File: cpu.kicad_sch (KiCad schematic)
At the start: 28 parts, among them J81 Conn_01x03_Pin, J82 Conn_Coaxial, J83 Conn_Coaxial, J84 Conn_01x02_Pin, SW81 SW_Push, SW82 SW_Push, U8 ESP32-C6-MINI-1U, U81 74HC595, U82 74HC595, U84 ISOW7842

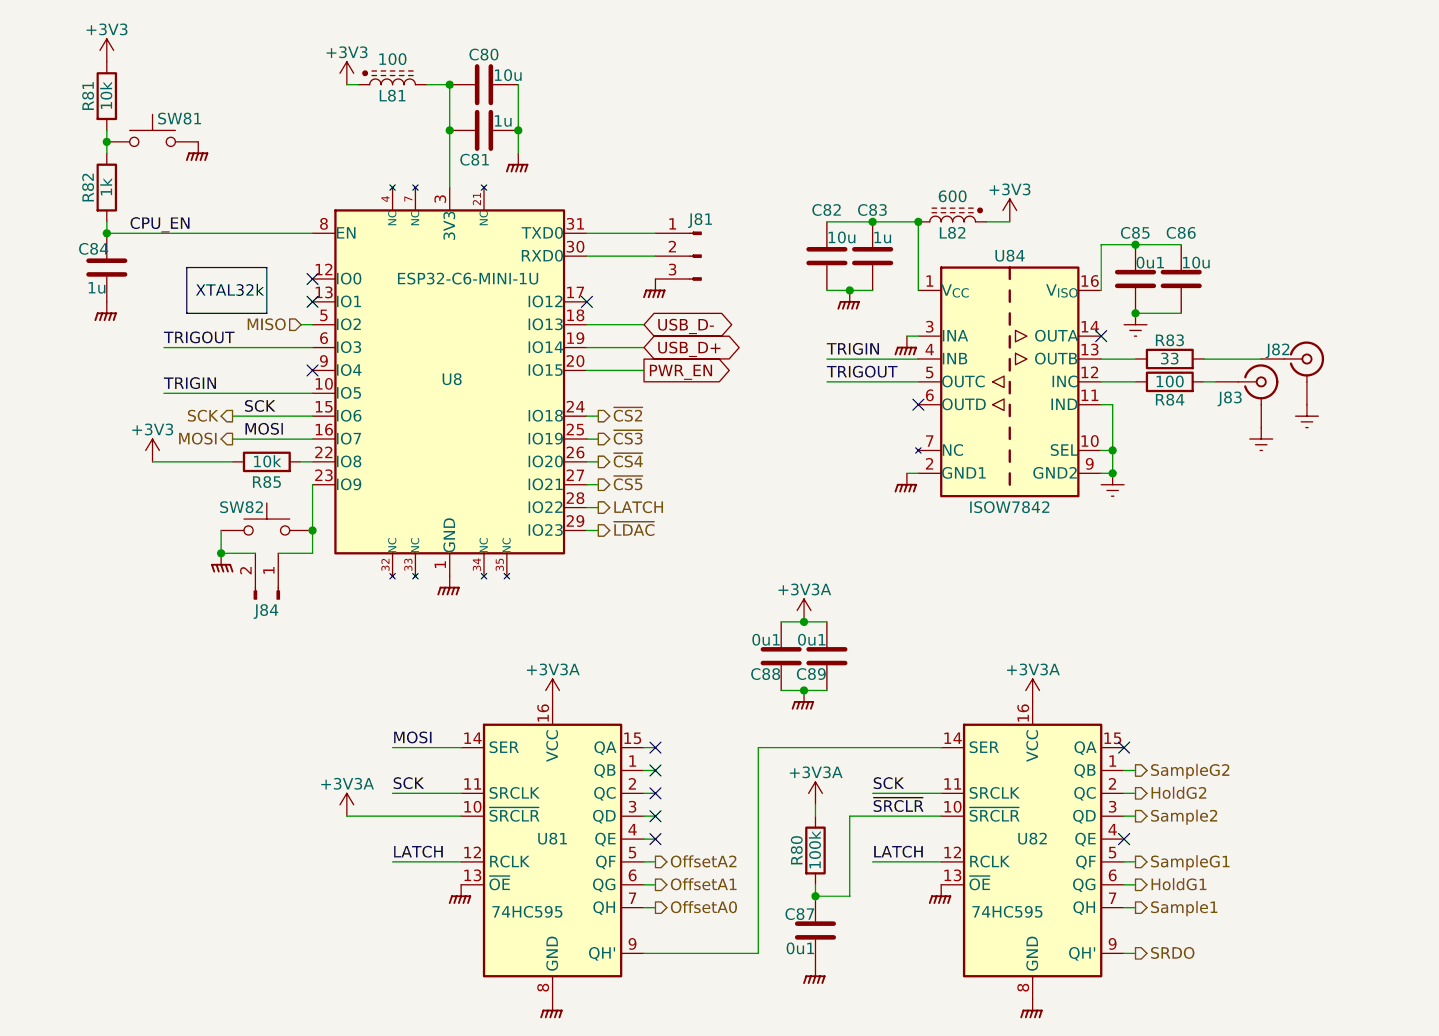
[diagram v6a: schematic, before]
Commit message: Power mostly routed
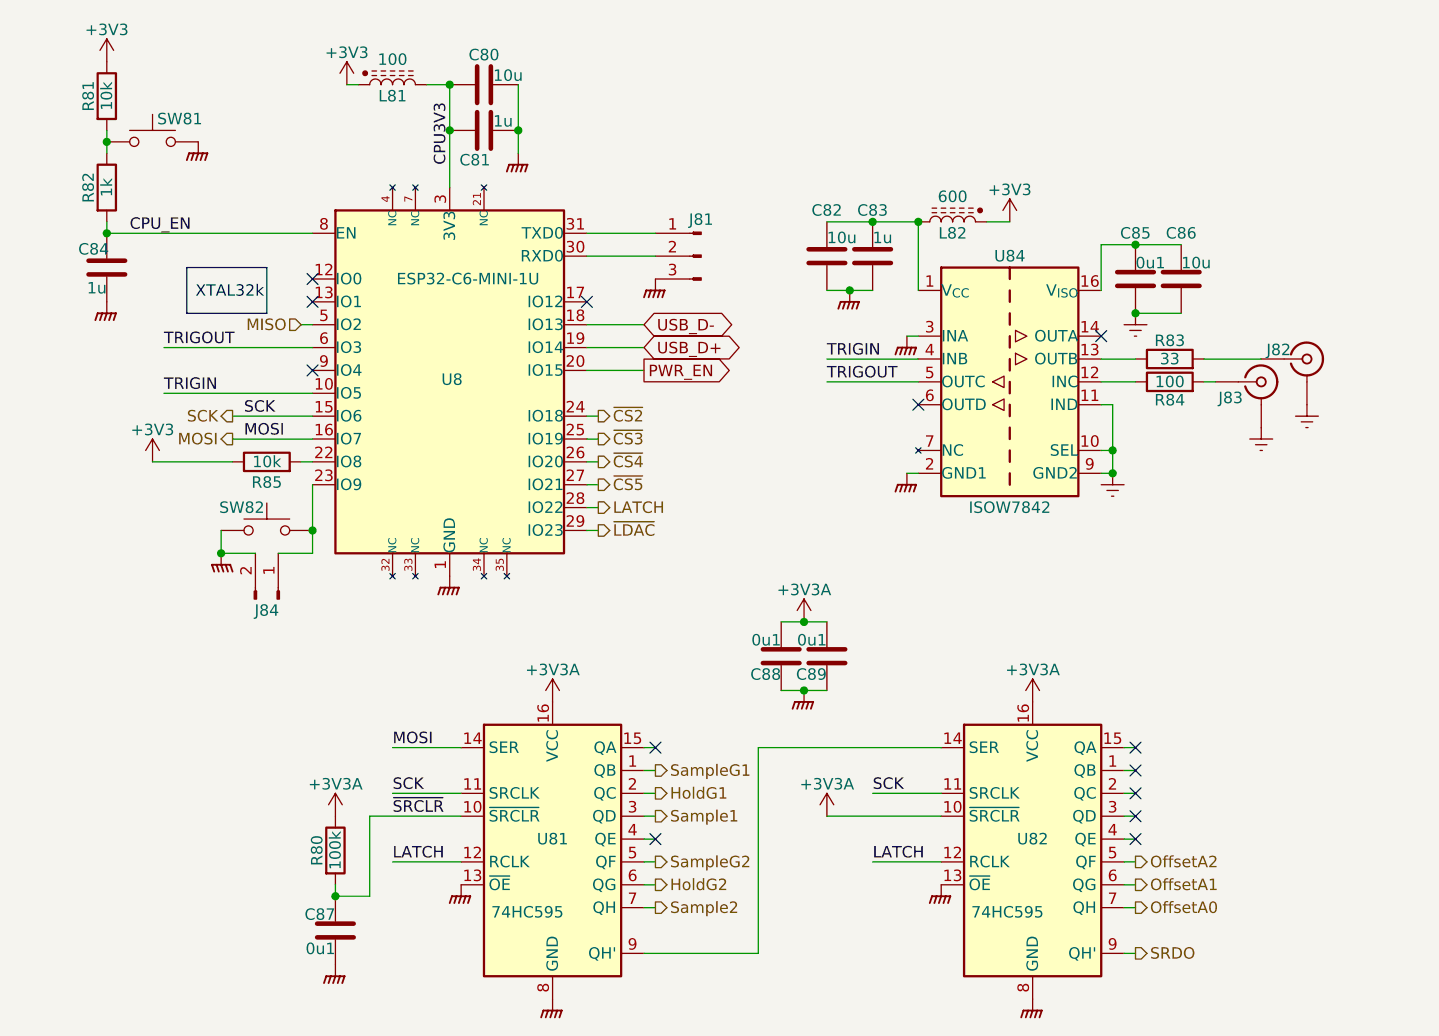
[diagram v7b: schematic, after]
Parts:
- renumbered U82 to U81, U81 to U82
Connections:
- net HoldG1: now also U81.2 (QC); no longer U81.6 (QG)
- net HoldG2: now also U81.6 (QG); no longer U81.2 (QC)
- net MOSI: now also U81.14 (SER); no longer U82.14 (SER)
- net SRDO: now also U82.9 (QH'); no longer U81.9 (QH')
- net Sample1: now also U81.3 (QD); no longer U81.7 (QH)
- net Sample2: now also U81.7 (QH); no longer U81.3 (QD)
- net SampleG1: now also U81.1 (QB); no longer U81.5 (QF)
- net SampleG2: now also U81.5 (QF); no longer U81.1 (QB)
- net CPU3V3: now reaches C80.1, C81.1, L81.2, U8.3 (3V3)
- new net: U81.9 (QH'), U82.14 (SER)
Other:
- moved on the sheet: C87, R80, U81, U82

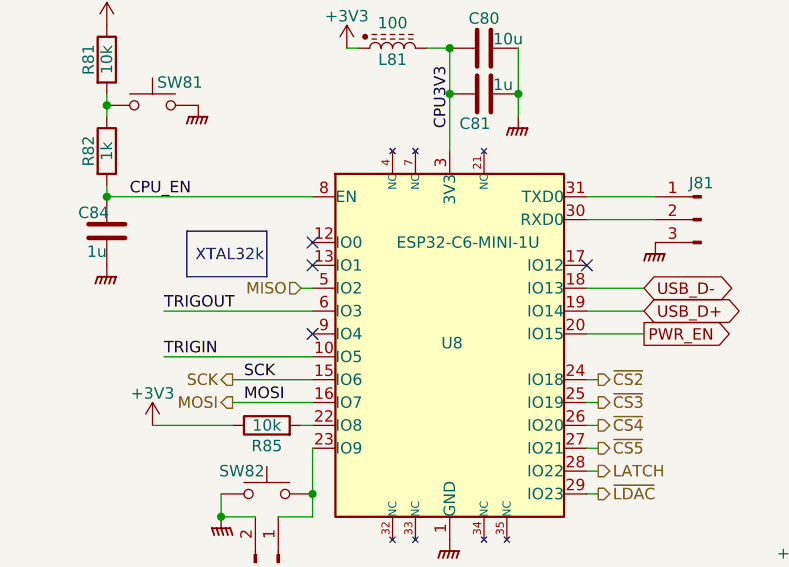
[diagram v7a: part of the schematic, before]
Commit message: Nearly all routed.  Repinning FDA resistors.
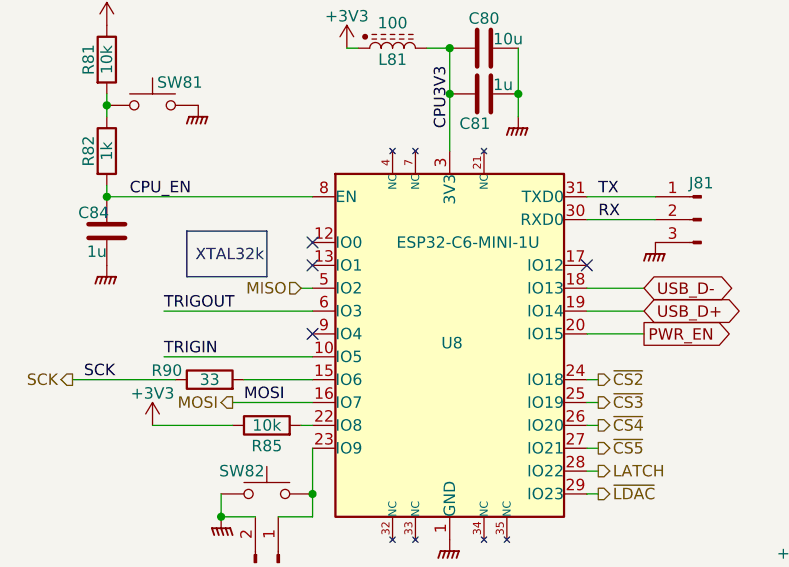
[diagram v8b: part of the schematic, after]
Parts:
- added R90: 33, Resistor_SMD:R_0402_1005Metric, symbol Device:R
- R80: LCSC (none) -> C25741
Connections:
- net SCK: now also R90.1; no longer U8.15 (IO6)
- net TX: now reaches J81.1 (Pin_1), U8.31 (TXD0)
- net RX: now reaches J81.2 (Pin_2), U8.30 (RXD0)
- new net: R90.2, U8.15 (IO6)
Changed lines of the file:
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@@
 	(wire
 		(pts
-			(xy 71.12 68.58) (xy 80.01 68.58)
+			(xy 53.34 68.58) (xy 64.77 68.58)
 		)
 		(stroke
@@
 	(wire
 		(pts
+			(xy 72.39 68.58) (xy 80.01 68.58)
+		)
+		(stroke
+			(width 0)
+			(type default)
+		)
+	)
+	(wire
+		(pts
 			(xy 110.49 81.28) (xy 111.76 81.28)
 		)
@@
 	)
 	(label "SCK"
-		(at 72.39 68.58 0)
+		(at 54.61 68.58 0)
 		(effects
 			(font
@@
 		)
 	)
+	(label "RX"
+		(at 111.76 50.8 0)
+		(effects
+			(font
+				(size 1.27 1.27)
+			)
+			(justify left bottom)
+		)
+	)
 	(label "SCK"
 		(at 142.24 110.49 0)
@@
 		)
 	)
+	(label "TX"
+		(at 111.76 48.26 0)
+		(effects
+			(font
+				(size 1.27 1.27)
+			)
+			(justify left bottom)
+		)
+	)
 	(label "TRIGOUT"
 		(at 137.16 64.77 0)
@@
 	(hierarchical_label "SCK"
 		(shape output)
-		(at 71.12 68.58 180)
+		(at 53.34 68.58 180)
 		(effects
 			(font
@@
 	)
 	(symbol
+		(lib_id "Device:R")
+		(at 68.58 68.58 90)
+		(unit 1)
+		(exclude_from_sim no)
+		(in_bom yes)
+		(on_board yes)
+		(dnp no)
+		(property "Reference" "R90"
+			(at 65.532 67.564 90)
+			(effects
+				(font
+					(size 1.27 1.27)
+				)
+				(justify left)
+			)
+		)
+		(property "Value" "33"
+			(at 68.58 68.58 90)
+			(effects
+				(font
+					(size 1.27 1.27)
+				)
+			)
+		)
+		(property "Footprint" "Resistor_SMD:R_0402_1005Metric"
+			(at 68.58 70.358 90)
+			(effects
+				(font
+					(size 1.27 1.27)
+				)
+				(hide yes)
+			)
+		)
+		(property "Datasheet" "~"
+			(at 68.58 68.58 0)
+			(effects
+				(font
+					(size 1.27 1.27)
+				)
+				(hide yes)
+			)
+		)
+		(property "Description" "Resistor"
+			(at 68.58 68.58 0)
+			(effects
+				(font
+					(size 1.27 1.27)
+				)
+				(hide yes)
+			)
+		)
+		(property "LCSC" "C25105"
+			(at 68.58 68.58 90)
+			(effects
+				(font
+					(size 1.27 1.27)
+				)
+				(hide yes)
+			)
+		)
+		(property "Stock" ""
+			(at 68.58 68.58 90)
+			(effects
+				(font
+					(size 1.27 1.27)
+				)
+				(hide yes)
+			)
+		)
+		(pin "2"
+		)
+		(pin "1"
+		)
+		(instances
+			(project "lincal"
+				(path "/b054cef4-39e3-49d8-aff0-7ba5a206c187/5e75b7d0-06d7-44d3-9715-75151d16c7a9"
+					(reference "R90")
+					(unit 1)
+				)
+			)
+		)
+	)
+	(symbol
 		(lib_id "74xx:74HC595")
 		(at 106.68 115.57 0)
@@
 			)
 		)
-		(property "LCSC" ""
+		(property "LCSC" "C25741"
 			(at 82.55 116.84 90)
 			(effects
